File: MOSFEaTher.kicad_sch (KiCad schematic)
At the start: 33 parts, among them J1 GPIO 13, J2 GPIO 12, J3 GPIO 27, J4 GPIO 21, J5 GPIO 33, J6 GPIO 15, J7 GPIO 32, J8 GPIO 14, Q1 STD7NK40Z, Q2 STD7NK40Z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

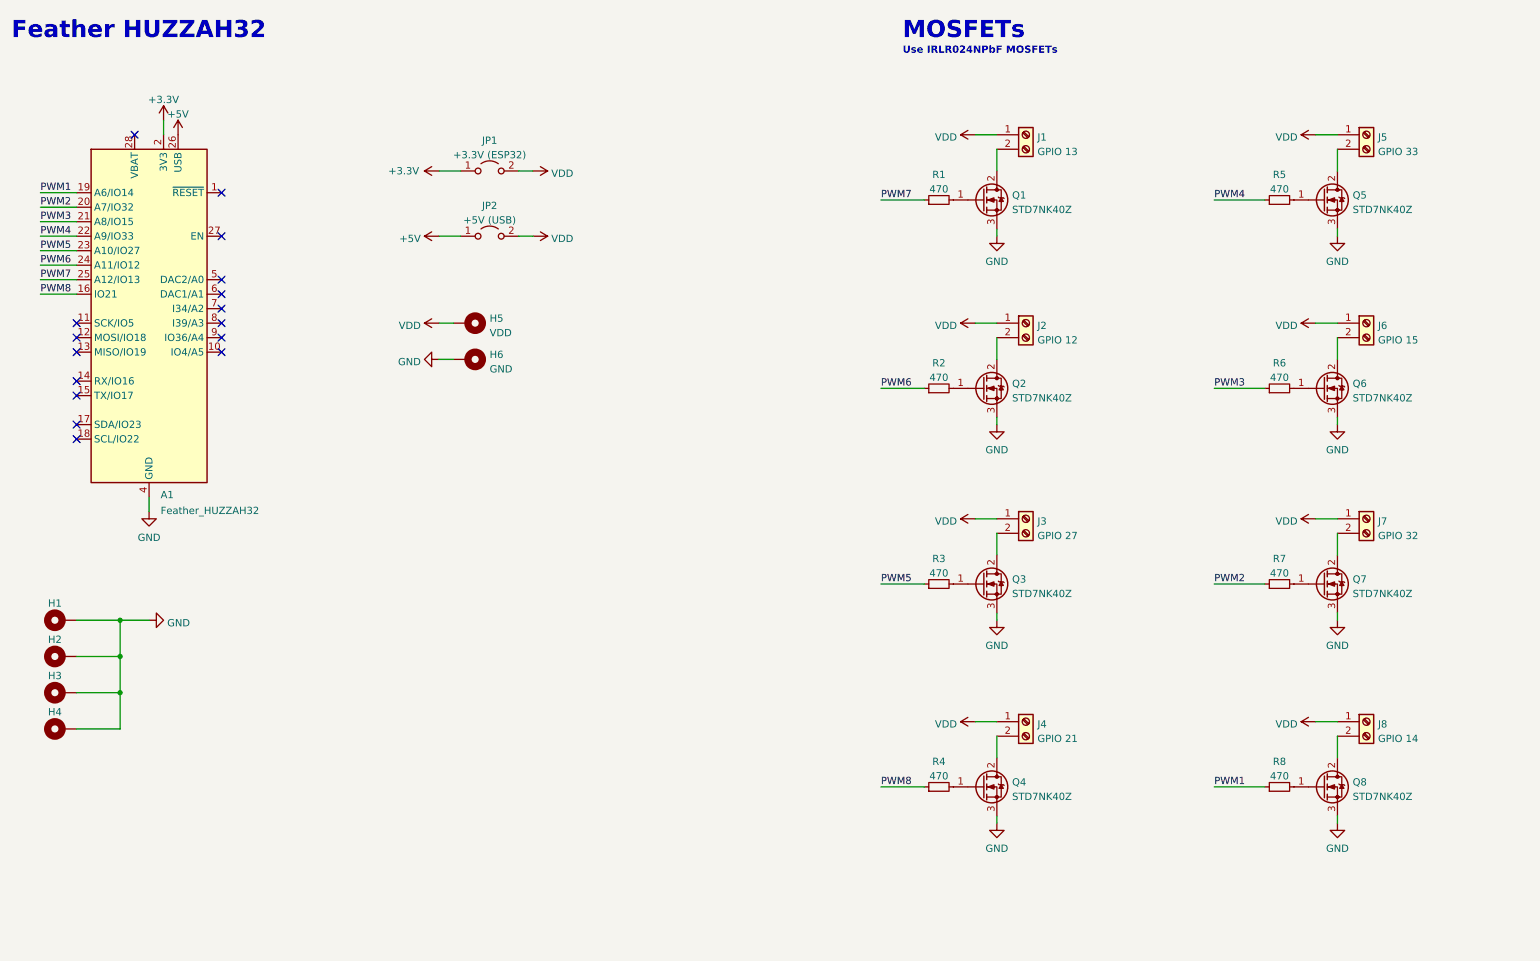
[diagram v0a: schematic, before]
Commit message: feat: M3 mounting holes, OSHW logo and THM affiliation
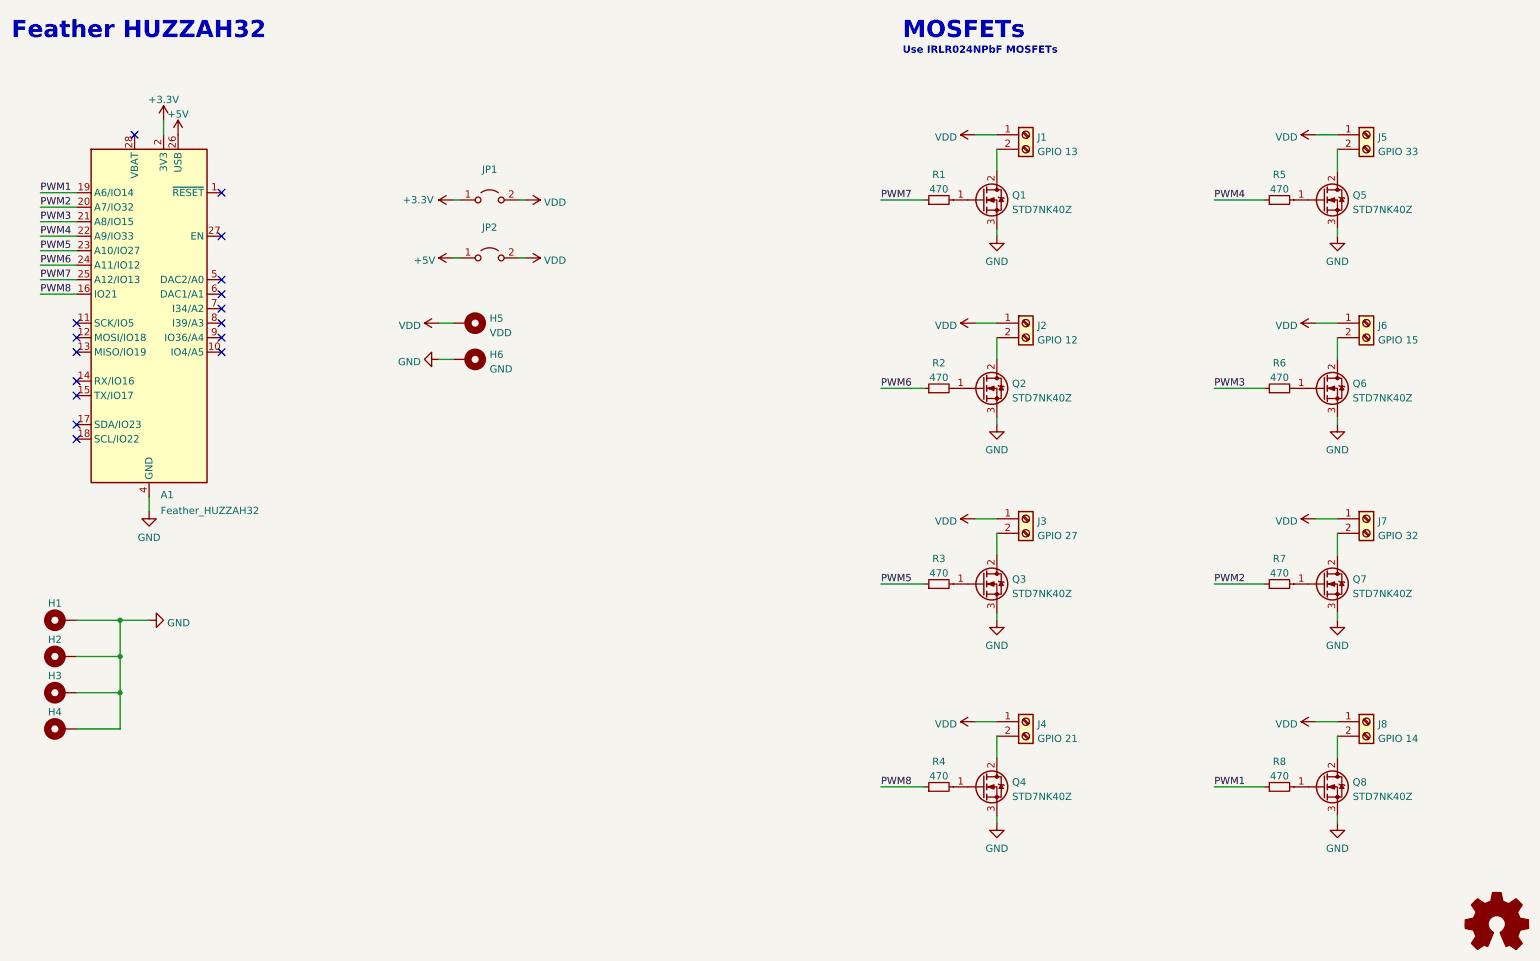
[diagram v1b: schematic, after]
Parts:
- H1, H2, H3, H4: footprint MountingHole:MountingHole_2.2mm_M2_DIN965_Pad -> MountingHole:MountingHole_3.2mm_M3_DIN965_Pad
- JP1: value +3.3V (ESP32) -> (none); footprint Connector_PinHeader_2.54mm:PinHeader_1x02_P2.54mm_Vertical -> Connector_PinHeader_2.54mm:PinHeader_2x01_P2.54mm_Vertical
- JP2: value +5V (USB) -> (none); footprint Connector_PinHeader_2.54mm:PinHeader_1x02_P2.54mm_Vertical -> Connector_PinHeader_2.54mm:PinHeader_2x01_P2.54mm_Vertical

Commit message: feat: better power and signal routing
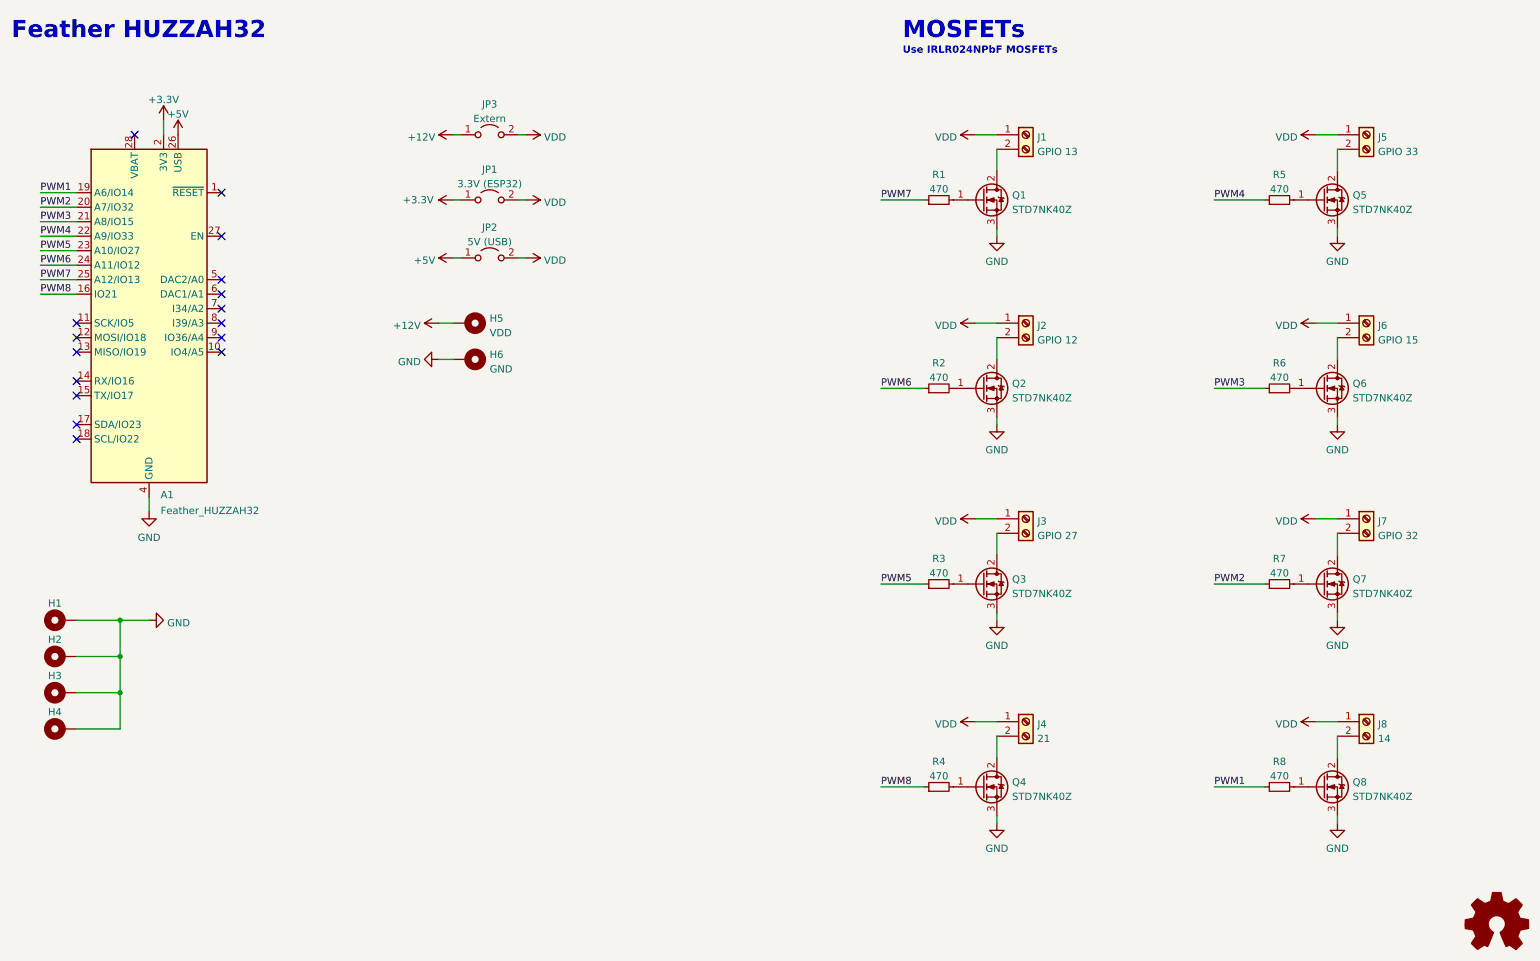
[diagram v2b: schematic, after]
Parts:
- added JP3: Extern, Connector_PinHeader_2.54mm:PinHeader_2x01_P2.54mm_Vertical, symbol Jumper:Jumper_2_Open
- J4: value GPIO 21 -> 21
- J8: value GPIO 14 -> 14
- JP1: value (none) -> 3.3V (ESP32)
- JP2: value (none) -> 5V (USB)
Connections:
- net VDD: now also JP3.2 (B); no longer H5.1
- new net +12V: H5.1, JP3.1 (A)
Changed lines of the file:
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@@
   (title_block
     (title "MOSFEaTher")
-    (date "2022-03-15")
-    (rev "02")
+    (date "2022-05-06")
+    (rev "03")
     (comment 1 "Author: Martin Weigel")
     (comment 4 "MOSFET board for the Adafruit HUZZAH32 (ESP32 Feather)")
@@
     (stroke (width 0) (type default) (color 0 0 0 0))
   )
+  (wire (pts (xy 105.41 35.56) (xy 106.68 35.56))
+    (stroke (width 0) (type default) (color 0 0 0 0))
+  )
   (wire (pts (xy 27.94 133.35) (xy 35.56 133.35))
     (stroke (width 0) (type default) (color 0 0 0 0))
@@
   )
   (wire (pts (xy 227.33 46.99) (xy 236.22 46.99))
+    (stroke (width 0) (type default) (color 0 0 0 0))
+  )
+  (wire (pts (xy 93.98 35.56) (xy 95.25 35.56))
     (stroke (width 0) (type default) (color 0 0 0 0))
   )
@@
       (effects (font (size 1.27 1.27)) (justify left))
     )
-    (property "Value" "GPIO 21" (id 1) (at 196.342 141.4022 0)
+    (property "Value" "21" (id 1) (at 196.342 141.4022 0)
       (effects (font (size 1.27 1.27)) (justify left))
     )
@@
     (pin "1")
   )
+  (symbol (lib_id "Jumper:Jumper_2_Open") (at 100.33 35.56 0) (unit 1)
+    (in_bom yes) (on_board yes) (fields_autoplaced)
+    (property "Reference" "JP3" (id 0) (at 100.33 30.2092 0))
+    (property "Value" "Extern" (id 1) (at 100.33 32.7461 0))
+    (property "Footprint" "Connector_PinHeader_2.54mm:PinHeader_2x01_P2.54mm_Vertical" (id 2) (at 100.33 35.56 0)
+      (effects (font (size 1.27 1.27)) hide)
+    )
+    (property "Datasheet" "~" (id 3) (at 100.33 35.56 0)
+      (effects (font (size 1.27 1.27)) hide)
+    )
+    (pin "1")
+    (pin "2")
+  )
   (symbol (lib_id "Mechanical:MountingHole_Pad") (at 25.4 139.7 90) (unit 1)
     (in_bom yes) (on_board yes) (fields_autoplaced)
@@
     (pin "2")
     (pin "3")
+  )
+  (symbol (lib_id "power:+12V") (at 93.98 35.56 90) (unit 1)
+    (in_bom yes) (on_board yes) (fields_autoplaced)
+    (property "Reference" "#PWR0102" (id 0) (at 97.79 35.56 0)
+      (effects (font (size 1.27 1.27)) hide)
+    )
+    (property "Value" "+12V" (id 1) (at 90.805 35.9938 90)
+      (effects (font (size 1.27 1.27)) (justify left))
+    )
+    (property "Footprint" "" (id 2) (at 93.98 35.56 0)
+      (effects (font (size 1.27 1.27)) hide)
+    )
+    (property "Datasheet" "" (id 3) (at 93.98 35.56 0)
+      (effects (font (size 1.27 1.27)) hide)
+    )
+    (pin "1")
   )
   (symbol (lib_id "Mechanical:MountingHole_Pad") (at 25.4 127 90) (unit 1)
@@
     (pin "3")
   )
+  (symbol (lib_id "power:VDD") (at 106.68 35.56 270) (unit 1)
+    (in_bom yes) (on_board yes) (fields_autoplaced)
+    (property "Reference" "#PWR0103" (id 0) (at 102.87 35.56 0)
+      (effects (font (size 1.27 1.27)) hide)
+    )
+    (property "Value" "VDD" (id 1) (at 109.855 35.9938 90)
+      (effects (font (size 1.27 1.27)) (justify left))
+    )
+    (property "Footprint" "" (id 2) (at 106.68 35.56 0)
+      (effects (font (size 1.27 1.27)) hide)
+    )
+    (property "Datasheet" "" (id 3) (at 106.68 35.56 0)
+      (effects (font (size 1.27 1.27)) hide)
+    )
+    (pin "1")
+  )
   (symbol (lib_id "power:GND") (at 248.92 156.21 0) (unit 1)
     (in_bom yes) (on_board yes) (fields_autoplaced)
@@
       (effects (font (size 1.27 1.27)) (justify left))
     )
-    (property "Value" "GPIO 14" (id 1) (at 256.032 141.4022 0)
+    (property "Value" "14" (id 1) (at 256.032 141.4022 0)
       (effects (font (size 1.27 1.27)) (justify left))
     )
@@
     (pin "1")
     (pin "2")
-  )
-  (symbol (lib_id "power:VDD") (at 91.44 68.58 90) (unit 1)
-    (in_bom yes) (on_board yes) (fields_autoplaced)
-    (property "Reference" "#PWR07" (id 0) (at 95.25 68.58 0)
-      (effects (font (size 1.27 1.27)) hide)
-    )
-    (property "Value" "VDD" (id 1) (at 88.265 69.0138 90)
-      (effects (font (size 1.27 1.27)) (justify left))
-    )
-    (property "Footprint" "" (id 2) (at 91.44 68.58 0)
-      (effects (font (size 1.27 1.27)) hide)
-    )
-    (property "Datasheet" "" (id 3) (at 91.44 68.58 0)
-      (effects (font (size 1.27 1.27)) hide)
-    )
-    (pin "1")
   )
   (symbol (lib_id "power:VDD") (at 185.42 102.87 90) (unit 1)
@@
     (in_bom yes) (on_board yes) (fields_autoplaced)
     (property "Reference" "JP1" (id 0) (at 100.33 41.6392 0))
-    (property "Value" "" (id 1) (at 100.33 44.1761 0))
+    (property "Value" "3.3V (ESP32)" (id 1) (at 100.33 44.1761 0))
     (property "Footprint" "Connector_PinHeader_2.54mm:PinHeader_2x01_P2.54mm_Vertical" (id 2) (at 100.33 46.99 0)
       (effects (font (size 1.27 1.27)) hide)
@@
     (in_bom yes) (on_board yes) (fields_autoplaced)
     (property "Reference" "JP2" (id 0) (at 100.33 51.7992 0))
-    (property "Value" "" (id 1) (at 100.33 54.3361 0))
+    (property "Value" "5V (USB)" (id 1) (at 100.33 54.3361 0))
     (property "Footprint" "Connector_PinHeader_2.54mm:PinHeader_2x01_P2.54mm_Vertical" (id 2) (at 100.33 57.15 0)
       (effects (font (size 1.27 1.27)) hide)
@@
     (pin "1")
   )
+  (symbol (lib_id "power:+12V") (at 91.44 68.58 90) (unit 1)
+    (in_bom yes) (on_board yes) (fields_autoplaced)
+    (property "Reference" "#PWR0104" (id 0) (at 95.25 68.58 0)
+      (effects (font (size 1.27 1.27)) hide)
+    )
+    (property "Value" "+12V" (id 1) (at 88.265 69.0138 90)
+      (effects (font (size 1.27 1.27)) (justify left))
+    )
+    (property "Footprint" "" (id 2) (at 91.44 68.58 0)
+      (effects (font (size 1.27 1.27)) hide)
+    )
+    (property "Datasheet" "" (id 3) (at 91.44 68.58 0)
+      (effects (font (size 1.27 1.27)) hide)
+    )
+    (pin "1")
+  )
   (symbol (lib_id "Connector:Screw_Terminal_01x02") (at 194.31 35.56 0) (unit 1)
     (in_bom yes) (on_board yes) (fields_autoplaced)
@@
       (reference "#PWR06") (unit 1) (value "+5V") (footprint "")
     )
-    (path "/c61ebf40-24d1-40cb-965c-2ed463d0af5b"
-      (reference "#PWR07") (unit 1) (value "VDD") (footprint "")
-    )
     (path "/9d154f18-38c4-48e9-a693-970456ad8e85"
       (reference "#PWR08") (unit 1) (value "GND") (footprint "")
@@
       (reference "#PWR0101") (unit 1) (value "VDD") (footprint "")
     )
+    (path "/4fe04c5e-8476-4135-bb9a-0b0bb7a270a2"
+      (reference "#PWR0102") (unit 1) (value "+12V") (footprint "")
+    )
+    (path "/8bdf5382-ae8a-4da0-a17e-8259042acf63"
+      (reference "#PWR0103") (unit 1) (value "VDD") (footprint "")
+    )
+    (path "/ef5a1cb8-c05c-4d68-a0b5-0ea9a073e0d0"
+      (reference "#PWR0104") (unit 1) (value "+12V") (footprint "")
+    )
     (path "/d1c959b2-6911-4815-9cf9-f6d32730e347"
       (reference "A1") (unit 1) (value "Feather_HUZZAH32") (footprint "Module:Adafruit_Feather")
@@
     )
     (path "/32e2065d-303c-44f1-ad96-669cc42eeae7"
-      (reference "J4") (unit 1) (value "GPIO 21") (footprint "TerminalBlock_Phoenix:TerminalBlock_Phoenix_MPT-0,5-2-2.54_1x02_P2.54mm_Horizontal")
+      (reference "J4") (unit 1) (value "21") (footprint "TerminalBlock_Phoenix:TerminalBlock_Phoenix_MPT-0,5-2-2.54_1x02_P2.54mm_Horizontal")
     )
     (path "/2438943e-b5a5-4c67-aa76-712886194fd1"
@@
     )
     (path "/959d4249-6f7d-4e27-a3c2-141ba04ecfd7"
-      (reference "J8") (unit 1) (value "GPIO 14") (footprint "TerminalBlock_Phoenix:TerminalBlock_Phoenix_MPT-0,5-2-2.54_1x02_P2.54mm_Horizontal")
+      (reference "J8") (unit 1) (value "14") (footprint "TerminalBlock_Phoenix:TerminalBlock_Phoenix_MPT-0,5-2-2.54_1x02_P2.54mm_Horizontal")
     )
     (path "/d2456fb5-2b99-45e1-9d17-eb9a485a3bd3"
@@
       (reference "JP2") (unit 1) (value "5V (USB)") (footprint "Connector_PinHeader_2.54mm:PinHeader_2x01_P2.54mm_Vertical")
     )
+    (path "/4362e6ac-6290-4071-922f-911c69fdd561"
+      (reference "JP3") (unit 1) (value "Extern") (footprint "Connector_PinHeader_2.54mm:PinHeader_2x01_P2.54mm_Vertical")
+    )
     (path "/2a72d102-5cc2-46a5-ba1d-7fad5fd13e56"
